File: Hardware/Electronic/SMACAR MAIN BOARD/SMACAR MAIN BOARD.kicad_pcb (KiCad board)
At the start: 2 copper layers, 13 parts, among them J2 USB_C_Receptacle_USB2.0_14P, U2 ESP32-S3-DevKitC

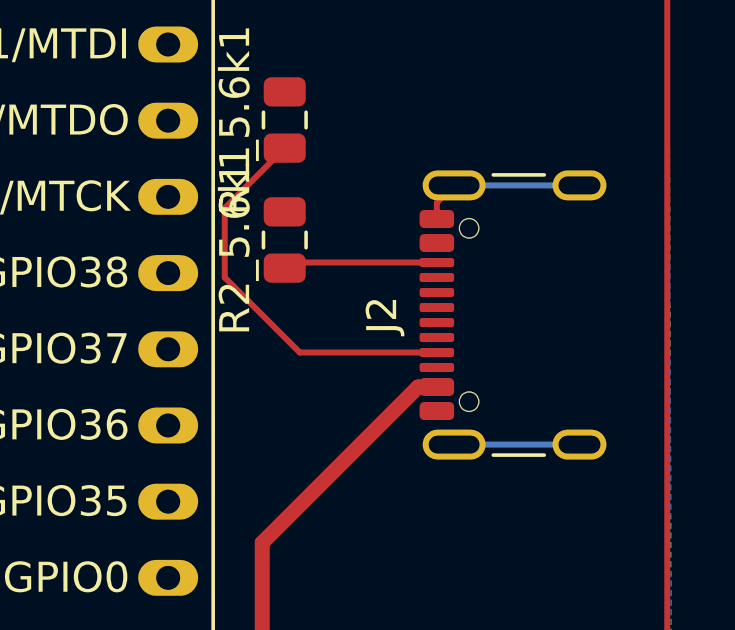
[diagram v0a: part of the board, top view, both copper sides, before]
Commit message: arreglos en las conexiones de usb c
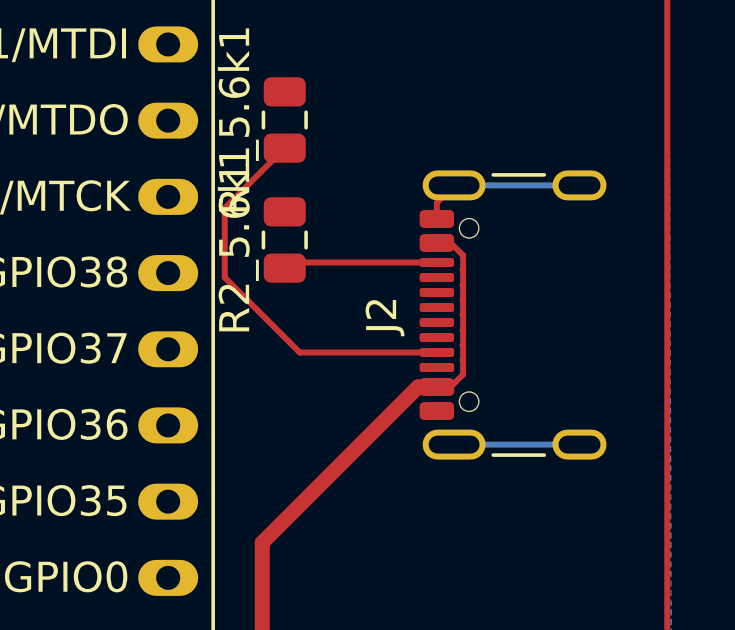
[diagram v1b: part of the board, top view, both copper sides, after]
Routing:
- net 5V: track 143.3 -> 149.4 mm
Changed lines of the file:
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@@
+	)
+	(segment
+		(start 153.696 55.517176)
+		(end 153.696 55.982824)
+		(width 0.2)
+		(layer "F.Cu")
+		(net 2)
+	)
+	(segment
+		(start 153.696 57.482824)
+		(end 153.678824 57.5)
+		(width 0.2)
+		(layer "F.Cu")
+		(net 2)
+	)
+	(segment
+		(start 153.696 55.982824)
+		(end 153.678824 56)
+		(width 0.2)
+		(layer "F.Cu")
+		(net 2)
+	)
+	(segment
+		(start 153.678824 58)
+		(end 153.696 58.017176)
+		(width 0.2)
+		(layer "F.Cu")
+		(net 2)
+	)
+	(segment
+		(start 153.678824 56.5)
+		(end 153.696 56.517176)
+		(width 0.2)
+		(layer "F.Cu")
+		(net 2)
+	)
+	(segment
+		(start 153.696 58.482824)
+		(end 153.678824 58.5)
+		(width 0.2)
+		(layer "F.Cu")
+		(net 2)
 	)
 	(segment
@@
 	)
 	(segment
+		(start 153.678824 57.5)
+		(end 153.696 57.517176)
+		(width 0.2)
+		(layer "F.Cu")
+		(net 2)
+	)
+	(segment
+		(start 153.696 58.017176)
+		(end 153.696 58.482824)
+		(width 0.2)
+		(layer "F.Cu")
+		(net 2)
+	)
+	(segment
+		(start 153.696 57.982824)
+		(end 153.678824 58)
+		(width 0.2)
+		(layer "F.Cu")
+		(net 2)
+	)
+	(segment
 		(start 152.82 59.4)
 		(end 152.1909 59.4)
@@
 	)
 	(segment
+		(start 153.696 58.517176)
+		(end 153.696 58.982824)
+		(width 0.2)
+		(layer "F.Cu")
+		(net 2)
+	)
+	(segment
 		(start 127.5 90.04)
 		(end 121 83.54)
@@
 	)
 	(segment
+		(start 153.278824 54.6)
+		(end 153.696 55.017176)
+		(width 0.2)
+		(layer "F.Cu")
+		(net 2)
+	)
+	(segment
 		(start 147 92.75)
 		(end 144.25 95.5)
@@
 	)
 	(segment
+		(start 153.678824 55.5)
+		(end 153.696 55.517176)
+		(width 0.2)
+		(layer "F.Cu")
+		(net 2)
+	)
+	(segment
+		(start 153.696 57.017176)
+		(end 153.696 57.482824)
+		(width 0.2)
+		(layer "F.Cu")
+		(net 2)
+	)
+	(segment
+		(start 153.696 57.517176)
+		(end 153.696 57.982824)
+		(width 0.2)
+		(layer "F.Cu")
+		(net 2)
+	)
+	(segment
 		(start 104 40.5)
 		(end 107 37.5)
@@
 	)
 	(segment
+		(start 153.696 55.482824)
+		(end 153.678824 55.5)
+		(width 0.2)
+		(layer "F.Cu")
+		(net 2)
+	)
+	(segment
 		(start 104 67)
 		(end 104 59.21)
@@
 	)
 	(segment
+		(start 153.278824 59.4)
+		(end 152.82 59.4)
+		(width 0.2)
+		(layer "F.Cu")
+		(net 2)
+	)
+	(segment
+		(start 153.696 58.982824)
+		(end 153.278824 59.4)
+		(width 0.2)
+		(layer "F.Cu")
+		(net 2)
+	)
+	(segment
+		(start 153.696 56.982824)
+		(end 153.678824 57)
+		(width 0.2)
+		(layer "F.Cu")
+		(net 2)
+	)
+	(segment
+		(start 153.678824 56)
+		(end 153.696 56.017176)
+		(width 0.2)
+		(layer "F.Cu")
+		(net 2)
+	)
+	(segment
 		(start 127.5 94)
 		(end 127.5 90.04)
@@
 	)
 	(segment
+		(start 153.678824 58.5)
+		(end 153.696 58.517176)
+		(width 0.2)
+		(layer "F.Cu")
+		(net 2)
+	)
+	(segment
+		(start 152.82 54.6)
+		(end 153.278824 54.6)
+		(width 0.2)
+		(layer "F.Cu")
+		(net 2)
+	)
+	(segment
+		(start 153.696 56.482824)
+		(end 153.678824 56.5)
+		(width 0.2)
+		(layer "F.Cu")
+		(net 2)
+	)
+	(segment
 		(start 104 76.54)
 		(end 104 67)
 		(width 0.2)
 		(layer "F.Cu")
+		(net 2)
+	)
+	(segment
+		(start 153.696 56.517176)
+		(end 153.696 56.982824)
+		(width 0.2)
+		(layer "F.Cu")
+		(net 2)
+	)
+	(segment
+		(start 153.678824 57)
+		(end 153.696 57.017176)
+		(width 0.2)
+		(layer "F.Cu")
+		(net 2)
+	)
+	(segment
+		(start 153.696 55.017176)
+		(end 153.696 55.482824)
+		(width 0.2)
+		(layer "F.Cu")
+		(net 2)
+	)
+	(segment
+		(start 153.696 56.017176)
+		(end 153.696 56.482824)
+		(width 0.2)
+		(layer "F.Cu")

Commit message: TVS
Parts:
- added U1: TVS0500DRV, Package_SON:WSON-6-1EP_2x2mm_P0.65mm_EP1x1.6mm, F.Cu at (112.4, 80.3)
- added U3: TVS0500DRV, Package_SON:WSON-6-1EP_2x2mm_P0.65mm_EP1x1.6mm, F.Cu at (112.1, 43.6)
- MOLEX1: value E-C SENSOR -> ELECTRICAL CONDUCTIVITY SENSOR
- MOLEX2: value PH -> M03PTH
- MOLEX3: value TDS SENSOR -> M03PTH
- MOLEX4: value TEMP -> M03PTH
- MOLEX5: value LORAWAN -> M04PTH
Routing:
- net Net-(R3_10k1-Pad2): track 39.7 -> 45.0 mm, vias 1 -> 2
- net 5V: track 149.4 -> 153.3 mm
- net GND: track 11.1 -> 12.4 mm

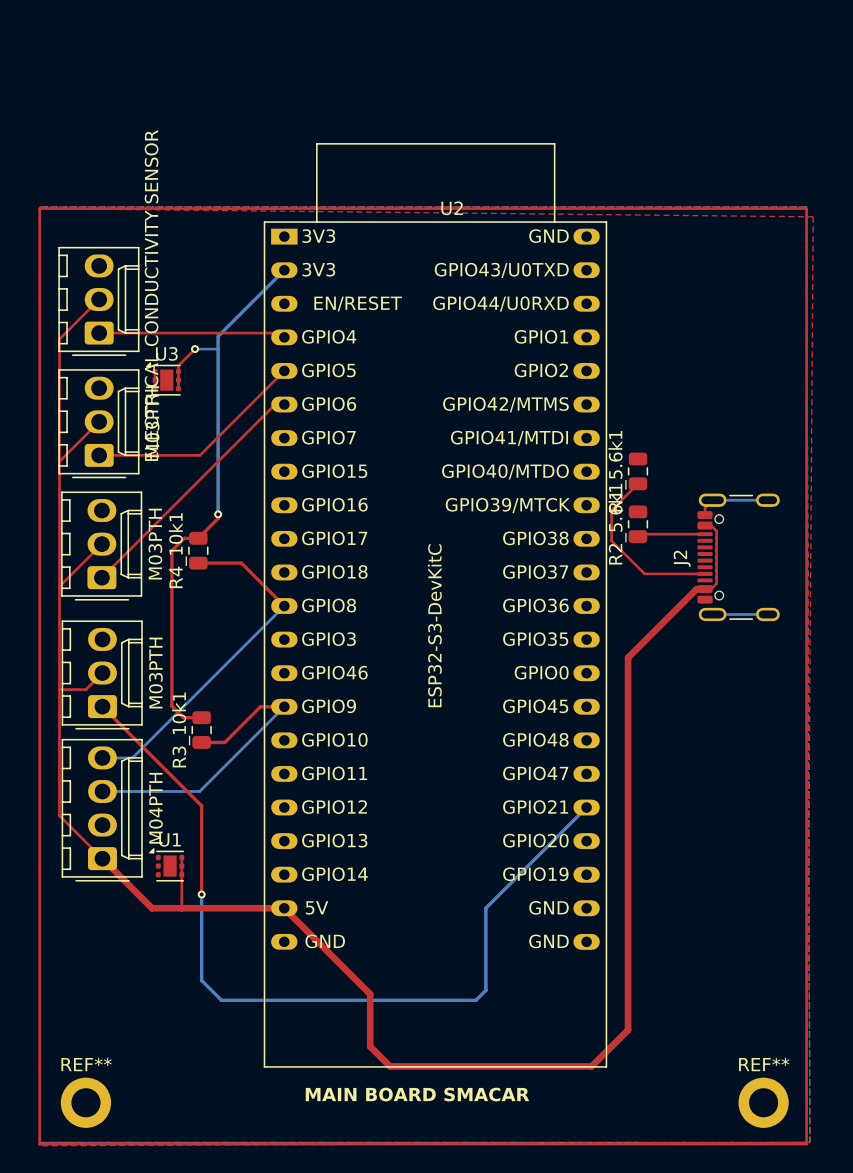
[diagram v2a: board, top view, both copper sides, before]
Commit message: Main Board Update
PCB Fix and Fabrication files generated
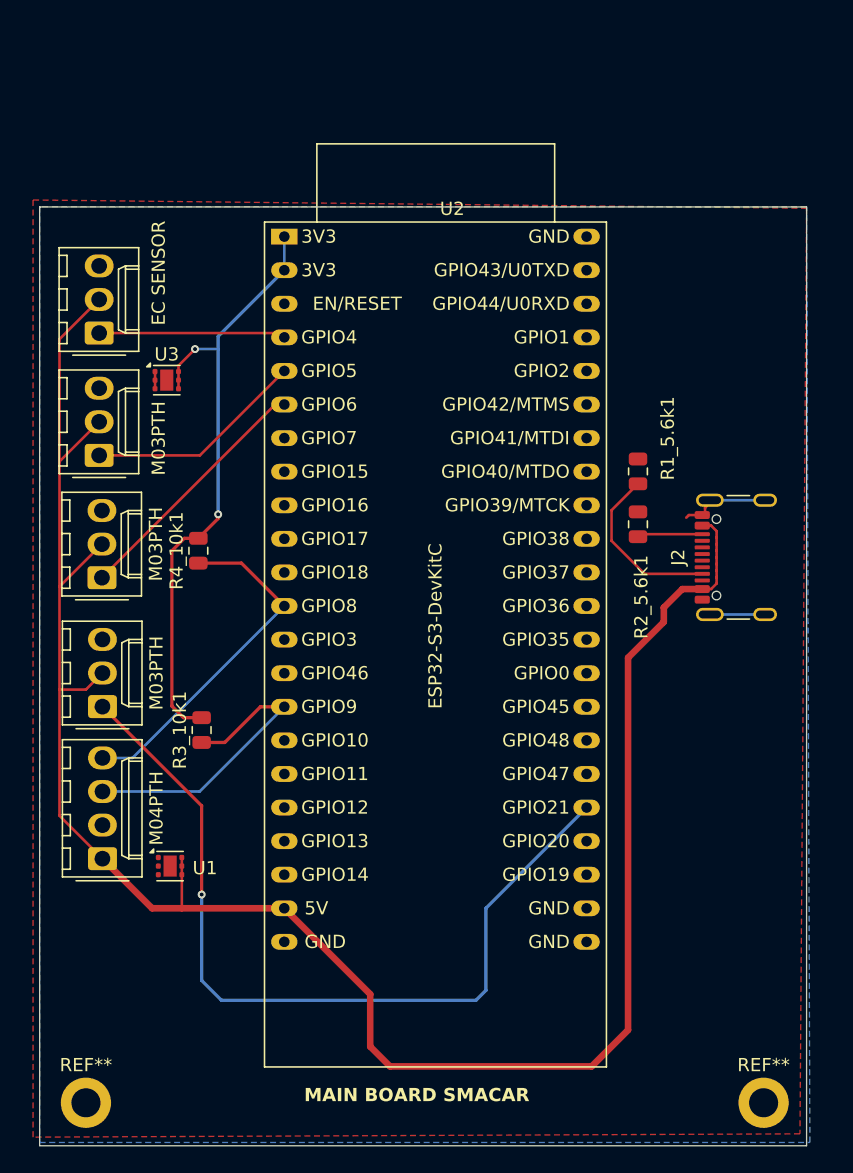
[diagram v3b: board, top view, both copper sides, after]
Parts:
- MOLEX1: value ELECTRICAL CONDUCTIVITY SENSOR -> EC SENSOR
- moved J2 0.21 mm to (156.3, 57.0)
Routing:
- net Net-(R3_10k1-Pad2): track 45.0 -> 47.5 mm
- net GND: track 12.4 -> 13.6 mm
- net 5V: track 153.3 -> 153.9 mm
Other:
- board outline added: 58 x 71 mm
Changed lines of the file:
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@@
 		(tags "resistor")
 		(property "Reference" "R2_5.6k1"
-			(at 0 -1.65 90)
+			(at -5.5 0.25 90)
 			(layer "F.SilkS")
 			(effects
@@
 		(tags "resistor")
 		(property "Reference" "R1_5.6k1"
-			(at 0 -1.65 90)
+			(at 2.5 2.25 90)
 			(layer "F.SilkS")
 			(effects
@@
 		)
 		(property "Value" "M03PTH"
-			(at 2.54 4.08 90)
+			(at 1.29 4.5 90)
 			(layer "F.SilkS")
 			(effects
@@
 		(tags "WSON NoLead")
 		(property "Reference" "U1"
-			(at 0 -1.95 0)
+			(at 2.6375 0.15 0)
 			(layer "F.SilkS")
 			(effects
@@
 	(footprint "Connector_USB:USB_C_Receptacle_GCT_USB4105-xx-A_16P_TopMnt_Horizontal"
 		(layer "F.Cu")
-		(at 156.5 57 90)
+		(at 156.29 57 90)
 		(descr "USB 2.0 Type C Receptacle, GCT, 16P, top mounted, horizontal, 5A: https://gct.co/files/drawings/usb4105.pdf")
 		(tags "USB C Type-C Receptacle SMD USB 2.0 16P 16C USB4105-15-A USB4105-15-A-060 USB4105-15-A-120 USB4105-GF-A USB4105-GF-A-060 USB4105-GF-A-120")
@@
 			)
 		)
-		(property "Value" "ELECTRICAL CONDUCTIVITY SENSOR"
-			(at 2.79 4 90)
+		(property "Value" "EC SENSOR"
+			(at 4.54 4.5 90)
 			(layer "F.SilkS")
 			(effects
@@
 	)
 	(gr_rect
-		(start 102.5 30.625)
-		(end 160.5 101.375)
+		(start 102.5 30.5)
+		(end 160.5 101.5)
 		(stroke
-			(width 0.2)
+			(width 0.05)
 			(type default)
 		)
 		(fill no)
-		(layer "F.Cu")
-		(net 1)
+		(layer "Edge.Cuts")
 	)
 	(gr_text "MAIN BOARD SMACAR"
@@
 	)
 	(segment
+		(start 151.6 53.8)
+		(end 151.4 54)
+		(width 0.2)
+		(layer "F.Cu")
+		(net 1)
+	)
+	(segment
 		(start 152.82 53.8)
 		(end 152.82 53.255)
@@
 	)
 	(segment
+		(start 152.61 53.8)
+		(end 151.6 53.8)
+		(width 0.2)
+		(layer "F.Cu")
+		(net 1)
+	)
+	(segment
 		(start 152.82 53.255)
 		(end 153.395 52.68)
@@
 	)
 	(segment
-		(start 129 95.5)
-		(end 127.5 94)
-		(width 0.5)
-		(layer "F.Cu")
-		(net 2)
-	)
-	(segment
-		(start 147 64.5909)
-		(end 147 92.75)
+		(start 152.82 59.4)
+		(end 151.1 59.4)
 		(width 0.5)
 		(layer "F.Cu")
@@
 	)
 	(segment
-		(start 144.25 95.5)
-		(end 129 95.5)
+		(start 149.7 61.8909)
+		(end 147 64.5909)
 		(width 0.5)
 		(layer "F.Cu")
@@
 	)
 	(segment
+		(start 147 92.75)
+		(end 144.25 95.5)
+		(width 0.5)
+		(layer "F.Cu")
+		(net 2)
+	)
+	(segment
 		(start 153.696 55.982824)
 		(end 153.678824 56)
@@
 	)
 	(segment
-		(start 152.1909 59.4)
-		(end 147 64.5909)
-		(width 0.5)
-		(layer "F.Cu")
-		(net 2)
-	)
-	(segment
 		(start 153.678824 57.5)
 		(end 153.696 57.517176)
@@
 	)
 	(segment
+		(start 129 95.5)
+		(end 127.5 94)
+		(width 0.5)
+		(layer "F.Cu")
+		(net 2)
+	)
+	(segment
 		(start 113.25 81)
 		(end 113.25 83.54)
@@
 	)
 	(segment
-		(start 152.82 59.4)
-		(end 152.1909 59.4)
-		(width 0.5)
-		(layer "F.Cu")
-		(net 2)
-	)
-	(segment
 		(start 121 83.54)
 		(end 113.25 83.54)
@@
 	)
 	(segment
-		(start 127.5 90.04)
-		(end 121 83.54)
+		(start 149.7 60.8)
+		(end 149.7 61.8909)
 		(width 0.5)
 		(layer "F.Cu")
@@
 	)
 	(segment
-		(start 147 92.75)
-		(end 144.25 95.5)
+		(start 147 64.5909)
+		(end 147 92.75)
 		(width 0.5)
 		(layer "F.Cu")
@@
 	)
 	(segment
+		(start 144.25 95.5)
+		(end 129 95.5)
+		(width 0.5)
+		(layer "F.Cu")
+		(net 2)
+	)
+	(segment
 		(start 153.696 58.982824)
 		(end 153.278824 59.4)
@@
 	)
 	(segment
-		(start 127.5 94)
-		(end 127.5 90.04)
+		(start 151.1 59.4)
+		(end 149.7 60.8)
+		(width 0.5)
+		(layer "F.Cu")
+		(net 2)
+	)
+	(segment
+		(start 127.5 90.04)
+		(end 121 83.54)
 		(width 0.5)
 		(layer "F.Cu")
@@
 	)
 	(segment
+		(start 127.5 94)
+		(end 127.5 90.04)
+		(width 0.5)
+		(layer "F.Cu")
+		(net 2)
+	)
+	(segment
 		(start 104 59.21)
 		(end 107.21 56)
@@
 		(net 46)
 	)
-	(zone
-		(net 1)
-		(net_name "GND")
-		(layer "F.Cu")
-		(hatch edge 0.5)
-		(priority 2)
-		(connect_pads
-			(clearance 0.5)
-		)
-		(min_thickness 0.25)
-		(filled_areas_thickness no)
-		(fill yes
-			(thermal_gap 0.5)
-			(thermal_bridge_width 0.5)
-		)
-		(polygon
-			(pts
-				(xy 102.5 30.5) (xy 160.5 30.5) (xy 160.75 101.25) (xy 102.5 101.25)
-			)
-		)
-	)
-	(zone
-		(net 1)
-		(net_name "GND")
-		(layer "F.Cu")
-		(hatch edge 0.5)
-		(connect_pads
-			(clearance 0.5)
-		)
-		(min_thickness 0.25)
-		(filled_areas_thickness no)
-		(fill yes
-			(thermal_gap 0.5)
-			(thermal_bridge_width 0.5)
-		)
-		(polygon
-			(pts
-				(xy 102.5 30.625) (xy 160.5 30.625) (xy 160.5 101.375) (xy 102.5 101.375)
-			)
-		)
+	(segment
+		(start 121.00368 32.74272)
+		(end 121.00368 35.28272)
+		(width 0.2)
+		(layer "B.Cu")
+		(net 46)
 	)
 	(zone
@@
 		(polygon
 			(pts
-				(xy 102.5 30.625) (xy 161 31.25) (xy 160.5 101.25) (xy 102.5 101.5)
+				(xy 102 29.975) (xy 160.5 30.6) (xy 160 100.6) (xy 102 100.85)
 			)
 		)

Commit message: V1.0 Revision
Revision for V1.0 of the project. Includes production files for JLCPCB. Some footprints and schematic symbols were changed.
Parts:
- removed R1_5.6k1, R2_5.6k1: 470R_0805_350mW, PCM_4ms_Resistor:R_0805_2012Metric
- removed U1, U3: TVS0500DRV, Package_SON:WSON-6-1EP_2x2mm_P0.65mm_EP1x1.6mm
- added D1: SMF33A, Diode_SMD:D_SMF, F.Cu at (150.5, 68.0)
- added D2: SMF33A, Diode_SMD:D_SMF, F.Cu at (117.0, 34.0)
- added R1_5.1k1: 470R_0805_350mW, Resistor_SMD:R_0805_2012Metric_Pad1.20x1.40mm_HandSolder, F.Cu at (154.5, 44.5)
- added R2_5.1k1: 470R_0805_350mW, Resistor_SMD:R_0805_2012Metric_Pad1.20x1.40mm_HandSolder, F.Cu at (153.0, 62.5)
- J2: value USB_C_Receptacle_USB2.0_14P -> 2137160001; footprint Connector_USB:USB_C_Receptacle_GCT_USB4105-xx-A_16P_TopMnt_Horizontal -> XUNPU TYPEC-306DDW-ARP16:MOLEX_2137160001
- R3_10k1, R4_10k1: footprint PCM_4ms_Resistor:R_0805_2012Metric -> Resistor_SMD:R_0805_2012Metric_Pad1.20x1.40mm_HandSolder
- moved J2 4.73 mm to (159.7, 53.7)
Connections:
- J2 pad A8: (no net) -> unconnected-(J2-SBU1-PadA8)
- J2 pad B8: (no net) -> unconnected-(J2-SBU2-PadB8)
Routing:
- net 5V: track 153.9 -> 178.0 mm, vias 0 -> 1
- net GND: track 13.6 -> 1.00 mm
- net Net-(J2-CC2): track 5.40 -> 15.3 mm
- net Net-(D2-A1): track 47.5 -> 46.3 mm, vias 2 -> 1
- net Net-(J2-CC1): track 13.5 -> 14.1 mm

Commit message: update
PCB Y CODIGO PROTOTIPO
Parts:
- removed D1: SMF33A, Diode_SMD:D_SMF
- removed R1_5.1k1, R2_5.1k1: 470R_0805_350mW, Resistor_SMD:R_0805_2012Metric_Pad1.20x1.40mm_HandSolder
- added REF**: MountingHole_2.2mm_M2_DIN965_Pad, MountingHole:MountingHole_2.2mm_M2_DIN965_Pad, F.Cu at (157.0, 34.0)
- J2: value 2137160001 -> Conn_01x02; footprint XUNPU TYPEC-306DDW-ARP16:MOLEX_2137160001 -> Connector_Molex:Molex_KK-254_AE-6410-02A_1x02_P2.54mm_Vertical
- MOLEX1: value EC SENSOR -> ECS
- moved J2 4.48 mm to (155.5, 52.2), turned to -90 degrees
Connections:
- U2 pad 27: TEMP SENSOR -> unconnected-(U2-GPIO21-Pad27)
- U2 pad 31: unconnected-(U2-GPIO0-Pad31) -> TEMP SENSOR
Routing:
- net 5V: track 178.0 -> 152.0 mm, vias 1 -> 0
- net Net-(J2-CC2): track 15.3 -> 0.00 mm
- net Net-(J2-CC1): track 14.1 -> 0.00 mm

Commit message: aaaaaaaaaaaaaaaaaa
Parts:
- MOLEX1: value ECS -> ELECTRICAL CONDUCTIVITY SENSOR
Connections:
- R3_10k1 pad 2: Net-(D2-A1) -> Net-(R1-Pad2)
- R4_10k1 pad 2: Net-(D2-A1) -> Net-(R1-Pad2)
- U2 pad 1: Net-(D2-A1) -> Net-(R1-Pad2)
- U2 pad 2: Net-(D2-A1) -> Net-(R1-Pad2)
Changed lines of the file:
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@@
 			(psa4output no)
 			(plot_black_and_white yes)
-			(plotinvisibletext no)
 			(sketchpadsonfab yes)
 			(plotpadnumbers yes)
@@
 	(net 39 "SCL")
 	(net 40 "Net-(D2-A1)")
+	(net 41 "Net-(R1-Pad2)")
 	(footprint "Connector_Molex:Molex_KK-254_AE-6410-04A_1x04_P2.54mm_Vertical"
 		(layer "F.Cu")
@@
 			(layers "F.Cu" "F.Mask" "F.Paste")
 			(roundrect_rratio 0.208333)
-			(net 40 "Net-(D2-A1)")
+			(net 41 "Net-(R1-Pad2)")
 			(pintype "passive")
 		)
@@
 			(layers "F.Cu" "F.Mask" "F.Paste")
 			(roundrect_rratio 0.208333)
-			(net 40 "Net-(D2-A1)")
+			(net 41 "Net-(R1-Pad2)")
 			(pintype "passive")
 		)
@@
 			(layers "*.Cu" "*.Mask")
 			(remove_unused_layers no)
-			(net 40 "Net-(D2-A1)")
+			(net 41 "Net-(R1-Pad2)")
 			(pinfunction "3V3")
 			(pintype "passive")
@@
 			(layers "*.Cu" "*.Mask")
 			(remove_unused_layers no)
-			(net 40 "Net-(D2-A1)")
+			(net 41 "Net-(R1-Pad2)")
 			(pinfunction "3V3")
 			(pintype "power_in")
@@
 			)
 		)
-		(property "Value" "ECS"
+		(property "Value" "ELECTRICAL CONDUCTIVITY SENSOR"
 			(at 4.54 4.5 90)
 			(layer "F.SilkS")

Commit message: cosillas
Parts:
- removed D2: SMF33A, Diode_SMD:D_SMF
- removed R3_10k1, R4_10k1: 470R_0805_350mW, Resistor_SMD:R_0805_2012Metric_Pad1.20x1.40mm_HandSolder
- added R1: 4.7k, Resistor_THT:R_Axial_DIN0204_L3.6mm_D1.6mm_P7.62mm_Horizontal, F.Cu at (110.2, 95.2)
- moved J2 38.0 mm to (156.8, 90.2)
- moved MOLEX5 11.8 mm to (106.5, 91.6)
- moved MOLEX4 9.26 mm to (106.8, 77.5)
- moved MOLEX3 7.26 mm to (106.8, 65.8)
- moved MOLEX2 4.54 mm to (107.0, 53.8)
- moved MOLEX1 1.25 mm to (107.0, 41.3)
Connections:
- MOLEX5 pad 3: SCL -> RX
- MOLEX5 pad 4: SDA -> Tx
- U2 pad 10: unconnected-(U2-GPIO17/ADC2_CH6-Pad10) -> Tx
- U2 pad 12: SDA -> unconnected-(U2-GPIO8/ADC1_CH7-Pad12)
- U2 pad 15: SCL -> unconnected-(U2-GPIO9/ADC1_CH8-Pad15)
- U2 pad 9: unconnected-(U2-GPIO16/ADC2_CH5/32K_N-Pad9) -> RX
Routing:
- net 5V: track 152.0 -> 0.00 mm
- net TEMP SENSOR: track 63.2 -> 0.00 mm, vias 1 -> 0
- net Net-(D2-A1): track 46.3 -> 0.00 mm, vias 1 -> 0
- net SDA: track 26.4 -> 0.00 mm
- net SCL: track 23.8 -> 0.00 mm
- net TDS SENSOR: track 19.2 -> 0.00 mm
- net PH SENSOR: track 16.6 -> 0.00 mm
- net ELECTRICAL CONDUCTIVITY: track 14.1 -> 0.00 mm
- net GND: track 1.00 -> 0.00 mm

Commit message: PCBS
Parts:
- added C1: 100nF_Ceramic, Capacitor_THT:C_Disc_D5.0mm_W2.5mm_P2.50mm, F.Cu at (117.0, 34.0)
- added C2: 100nF_Ceramic, Capacitor_THT:C_Disc_D5.0mm_W2.5mm_P2.50mm, F.Cu at (112.8, 57.5)
- added C3: 100nF_Ceramic, Capacitor_THT:C_Disc_D5.0mm_W2.5mm_P2.50mm, F.Cu at (113.0, 69.5)
- moved R1 62.3 mm to (158.0, 55.3), turned to 90 degrees
- moved MOLEX4 53.5 mm to (157.5, 60.5), turned to -90 degrees
- moved U2 7.14 mm to (128.1, 32.7)
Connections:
- MOLEX4 pad 2: 5V -> 3.3V
- R1 pad 2: Net-(R1-Pad2) -> 3.3V
- U2 pad 1: Net-(R1-Pad2) -> 3.3V
- U2 pad 2: Net-(R1-Pad2) -> 3.3V
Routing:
- net 5V: track 0.00 -> 128.0 mm
- net 3.3V: track 0.00 -> 120.8 mm
- net RX: track 0.00 -> 45.0 mm
- net Tx: track 0.00 -> 38.8 mm
- net TDS SENSOR: track 0.00 -> 36.5 mm
- net PH SENSOR: track 0.00 -> 29.4 mm
- net ELECTRICAL CONDUCTIVITY: track 0.00 -> 29.2 mm
- net TEMP SENSOR: track 0.00 -> 18.2 mm
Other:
- board outline removed
